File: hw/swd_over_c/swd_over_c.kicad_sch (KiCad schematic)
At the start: 16 parts, among them J1 USB_C_Receptacle_USB2.0, J2 Conn_ARM_JTAG_SWD_10, P1 USB_C_Plug, U1 ATtiny24-20M

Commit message: Somehow got the values for R4 and R5 swapped...
Swapped them in schematic and in code (manually reworked v1.6 boards to swap R4/R5)
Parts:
- R4: value 56k -> 10k; MPN RC0402FR-0756KL -> RC0402FR-0710KL; Vendor Part Number 311-56.0KLRCT-ND -> 311-10.0KLRCT-ND
- R5: value 10k -> 56k; MPN RC0402FR-0710KL -> RC0402FR-0756KL; Vendor Part Number 311-10.0KLRCT-ND -> 311-56.0KLRCT-ND
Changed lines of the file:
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@@
   (title_block
     (title "Debugotron - SWD2USBC")
-    (date "2022-05-15")
-    (rev "1.4")
+    (date "2022-06-07")
+    (rev "1.7")
     (company "Quesadillon LLC")
   )
@@
     (in_bom yes) (on_board yes)
     (property "Reference" "R5" (id 0) (at 180.34 67.31 90))
-    (property "Value" "10k" (id 1) (at 180.34 71.12 90))
+    (property "Value" "56k" (id 1) (at 180.34 71.12 90))
     (property "Footprint" "Resistor_SMD:R_0402_1005Metric" (id 2) (at 180.34 73.66 0)
       (effects (font (size 1.27 1.27)) hide)
@@
       (effects (font (size 1.27 1.27)) hide)
     )
-    (property "Description" "RES 10K OHM 1% 1/16W 0402" (id 4) (at 180.34 73.66 0)
+    (property "Description" "RES 56K OHM 1% 1/16W 0402" (id 4) (at 180.34 73.66 0)
       (effects (font (size 1.27 1.27)) hide)
     )
@@
       (effects (font (size 1.27 1.27)) hide)
     )
-    (property "MPN" "RC0402FR-0710KL" (id 6) (at 180.34 73.66 0)
+    (property "MPN" "RC0402FR-0756KL" (id 6) (at 180.34 73.66 0)
       (effects (font (size 1.27 1.27)) hide)
     )
@@
       (effects (font (size 1.27 1.27)) hide)
     )
-    (property "Vendor Part Number" "311-10.0KLRCT-ND" (id 9) (at 180.34 73.66 0)
+    (property "Vendor Part Number" "311-56.0KLRCT-ND" (id 9) (at 180.34 73.66 0)
       (effects (font (size 1.27 1.27)) hide)
     )
@@
     (in_bom yes) (on_board yes)
     (property "Reference" "R4" (id 0) (at 180.34 66.04 90))
-    (property "Value" "56k" (id 1) (at 180.34 63.5 90))
+    (property "Value" "10k" (id 1) (at 180.34 63.5 90))
     (property "Footprint" "Resistor_SMD:R_0402_1005Metric" (id 2) (at 180.34 60.96 0)
       (effects (font (size 1.27 1.27)) hide)
@@
       (effects (font (size 1.27 1.27)) hide)
     )
-    (property "Description" "RES 56K OHM 1% 1/16W 0402" (id 4) (at 180.34 60.96 0)
+    (property "Description" "RES 10K OHM 1% 1/16W 0402" (id 4) (at 180.34 60.96 0)
       (effects (font (size 1.27 1.27)) hide)
     )
@@
       (effects (font (size 1.27 1.27)) hide)
     )
-    (property "MPN" "RC0402FR-0756KL" (id 6) (at 180.34 60.96 0)
+    (property "MPN" "RC0402FR-0710KL" (id 6) (at 180.34 60.96 0)
       (effects (font (size 1.27 1.27)) hide)
     )
@@
       (effects (font (size 1.27 1.27)) hide)
     )
-    (property "Vendor Part Number" "311-56.0KLRCT-ND" (id 9) (at 180.34 60.96 0)
+    (property "Vendor Part Number" "311-10.0KLRCT-ND" (id 9) (at 180.34 60.96 0)
       (effects (font (size 1.27 1.27)) hide)
     )
@@
     )
     (path "/58dcbd1f-c6fe-4c32-b2f3-448aeeb2a148"
-      (reference "R4") (unit 1) (value "56k") (footprint "Resistor_SMD:R_0402_1005Metric")
+      (reference "R4") (unit 1) (value "10k") (footprint "Resistor_SMD:R_0402_1005Metric")
     )
     (path "/4270b08b-df31-4c02-8549-8caf041f455d"
-      (reference "R5") (unit 1) (value "10k") (footprint "Resistor_SMD:R_0402_1005Metric")
+      (reference "R5") (unit 1) (value "56k") (footprint "Resistor_SMD:R_0402_1005Metric")
     )
     (path "/28b61970-be32-4027-a006-7ee2adc035c1"

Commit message: v2.0 SWD Over C
Going to a different MCU since it's available at JLC and both USB-C connectors instead of plugs.
_maybe_ this will work with a short USBC cable with all the conductors and make things much easier
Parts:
- removed J1: USB_C_Receptacle_USB2.0, alvarop:USB4500-03, symbol Connector:USB_C_Receptacle_USB2.0
- removed P1: USB_C_Plug, alvarop:‎USB4155-03-C‎, symbol Connector:USB_C_Plug
- added J1, J3: USB_C_Receptacle, alvarop:MOLEX-1054500101, symbol Connector:USB_C_Receptacle
- U1: footprint ultralibrarian:ATTINY24A-MMH_MOD -> ultralibrarian:ATTINY24A-MU; MPN ATTINY24A-MMH -> ATTINY24A-MU; Vendor Part Number ATTINY24A-MMH-ND -> ATTINY24A-MU-ND
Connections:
- net CC1: now also J3.A5 (CC1)
- net CC1_IN_MOSI: now also J1.A5 (CC1)
- net CC1_R1: now also U1.5 (AREF/PA0); no longer U1.11 (XTAL1/PB0)
- net CC1_R2: now also U1.4 (PA1); no longer U1.12 (XTAL2/PB1)
- net CC2: now also J3.B5 (CC2)
- net CC2_IN_MISO: now also J1.B5 (CC2)
- net CC2_R1: now also U1.12 (XTAL2/PB1); no longer U1.4 (PA1)
- net CC2_R2: now also U1.11 (XTAL1/PB0); no longer U1.5 (AREF/PA0)
- net D+: now also J1.A6 (D+), J1.B6 (D+), J3.A6 (D+), J3.B6 (D+)
- net D-: now also J1.A7 (D-), J1.B7 (D-), J3.A7 (D-), J3.B7 (D-)
- net GND: now also J1.A1 (GND), J1.A12 (GND), J1.B1 (GND), J1.B12 (GND), J3.A1 (GND), J3.A12 (GND), J3.B1 (GND), J3.B12 (GND)
- net MCURST: now also J1.B8 (SBU2)
- net NRST: now also J3.A11 (RX2+)
- net SBU1: now also J3.A8 (SBU1)
- net SBU2: now also J3.B8 (SBU2)
- net SCK: now also J1.A8 (SBU1)
- net SHIELD: now also J1.S1 (SHIELD), J3.S1 (SHIELD)
- net SWDCLK: now also J3.B10 (RX1-)
- net SWDIO: now also J3.B11 (RX1+)
- net SWO: now also J3.A10 (RX2-)
- net VBUS: now also J1.A4 (VBUS), J1.A9 (VBUS), J1.B4 (VBUS), J1.B9 (VBUS), J3.A4 (VBUS), J3.A9 (VBUS), J3.B4 (VBUS), J3.B9 (VBUS)

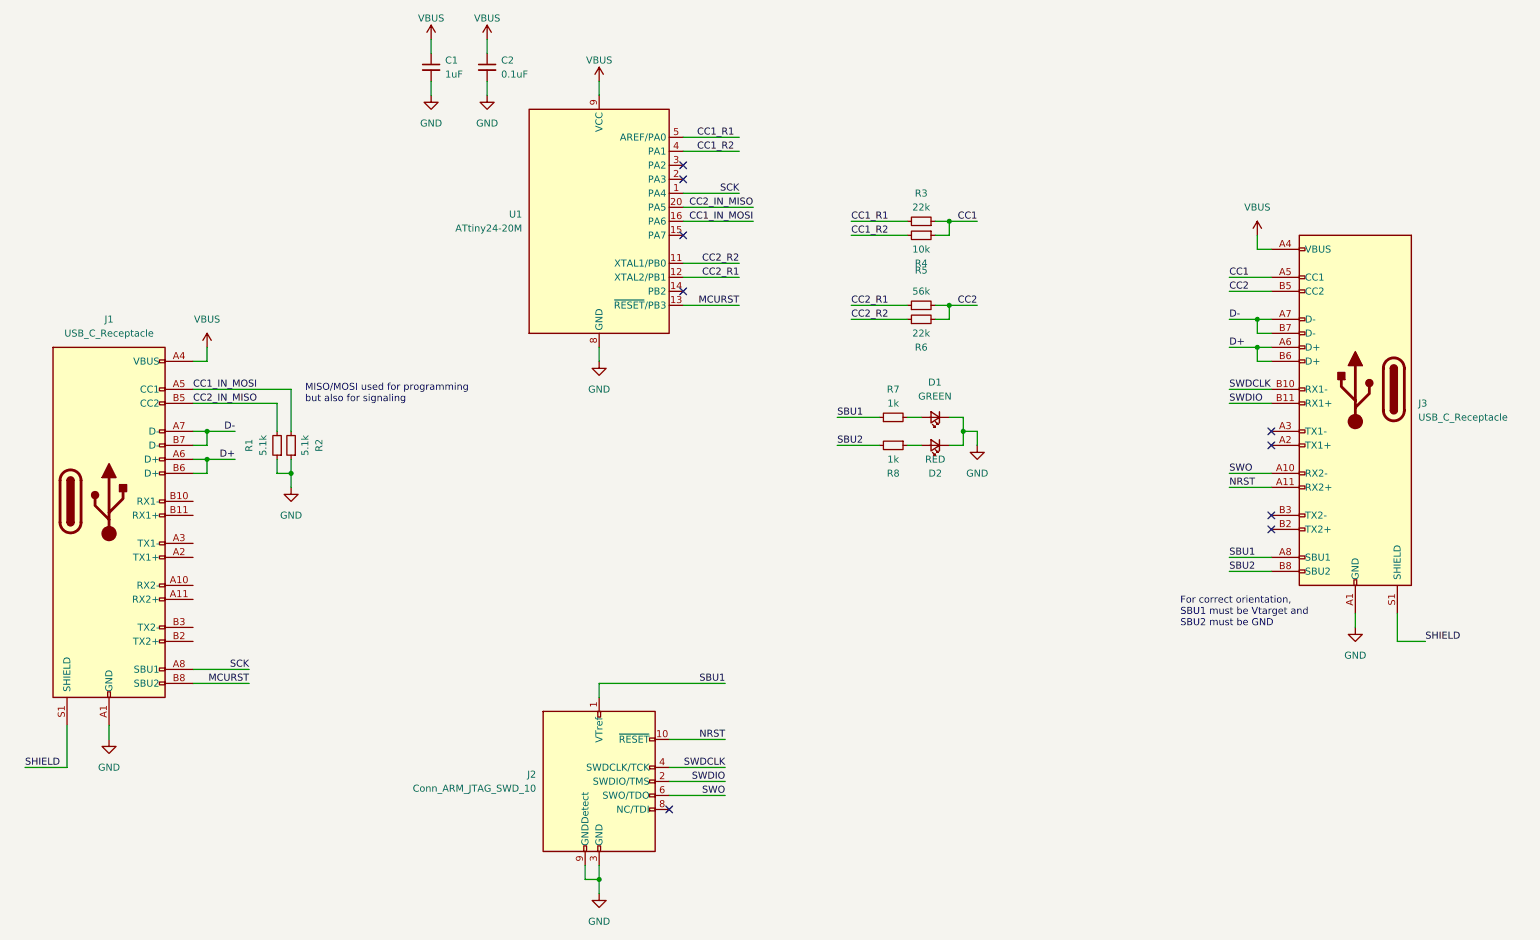
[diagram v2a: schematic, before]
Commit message: v3.0 SWD2USBC
Had the tx/rx pairs flipped since I switched from USB-C Plug to Connector...
Removed MCU since cables don't connect both CC1/CC2 so can't actually do a proper debug accessory mode.
Should still work though?
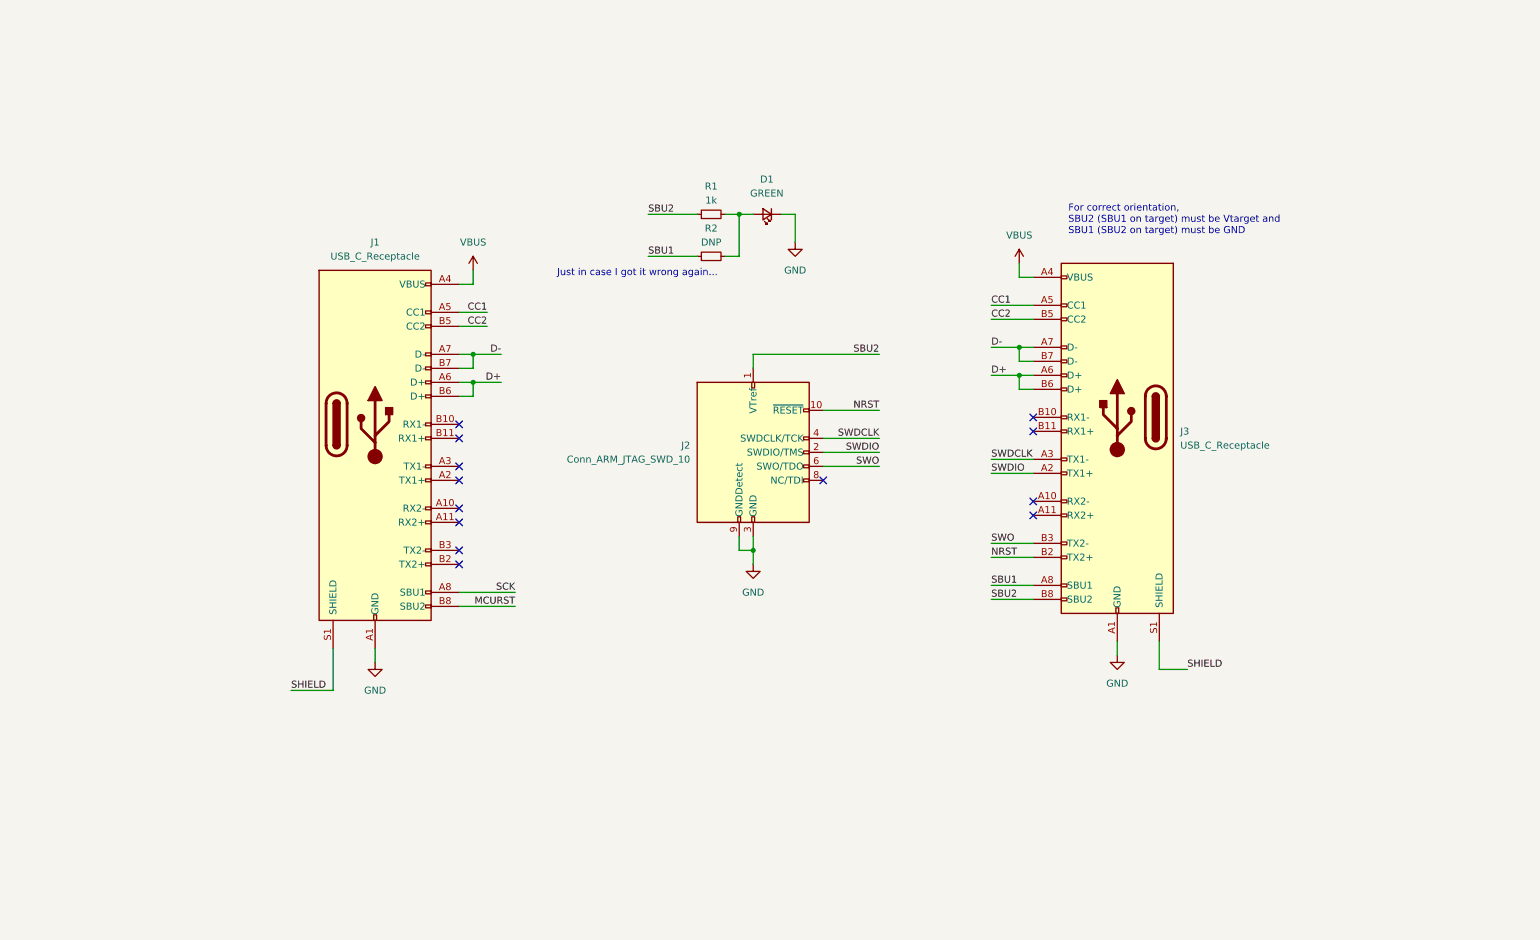
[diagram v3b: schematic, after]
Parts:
- removed C1: 1uF, Capacitor_SMD:C_0402_1005Metric, symbol Device:C_Small
- removed C2: 0.1uF, Capacitor_SMD:C_0402_1005Metric, symbol Device:C_Small
- removed D2: RED, LED_SMD:LED_0603_1608Metric, symbol Device:LED_Small
- removed R1: 5.1k, Resistor_SMD:R_0402_1005Metric, symbol Device:R_Small
- removed R3, R6: 22k, Resistor_SMD:R_0402_1005Metric, symbol Device:R_Small
- removed R4: 10k, Resistor_SMD:R_0402_1005Metric, symbol Device:R_Small
- removed R5: 56k, Resistor_SMD:R_0402_1005Metric, symbol Device:R_Small
- removed R8: 1k, Resistor_SMD:R_0402_1005Metric, symbol Device:R_Small
- removed U1: ATtiny24-20M, ultralibrarian:ATTINY24A-MU, symbol MCU_Microchip_ATtiny:ATtiny24-20M
- R2: value 5.1k -> DNP; MPN RC0402FR-075K1L -> RC0402FR-071KL; Vendor Part Number 311-5.1KJRCT-ND -> 311-1.00KLRCT-ND
- renumbered R7 to R1
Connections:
- net CC2_IN_MISO is gone; now on net CC2: J1.B5 (CC2)
- net CC1: now also J1.A5 (CC1)
- net GND: no longer R2.1
- net NRST: now also J3.B2 (TX2+); no longer J3.A11 (RX2+)
- net SBU1: now also R2.1; no longer J2.1 (VTref), R1.1
- net SBU2: now also J2.1 (VTref), R1.1
- net SWDCLK: now also J3.A3 (TX1-); no longer J3.B10 (RX1-)
- net SWDIO: now also J3.A2 (TX1+); no longer J3.B11 (RX1+)
- net SWO: now also J3.B3 (TX2-); no longer J3.A10 (RX2-)
- net at D1.2 (A), R1.2: now also R2.2
- removed net CC1_IN_MOSI: J1.A5 (CC1), R2.2
- no-connect marks 9 -> 13
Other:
- note added: "For correct orientation, SBU2 (SBU1 on target) must be Vtarget and SBU1 (SBU2 on target) must be GND"
- note added: "Just in case I got it wrong again..."
- note removed: "For correct orientation, SBU1 must be Vtarget and SBU2 must be GND"
- note removed: "MISO/MOSI used for programming but also for signaling"
- moved on the sheet: D1, J1, J2, J3, R1

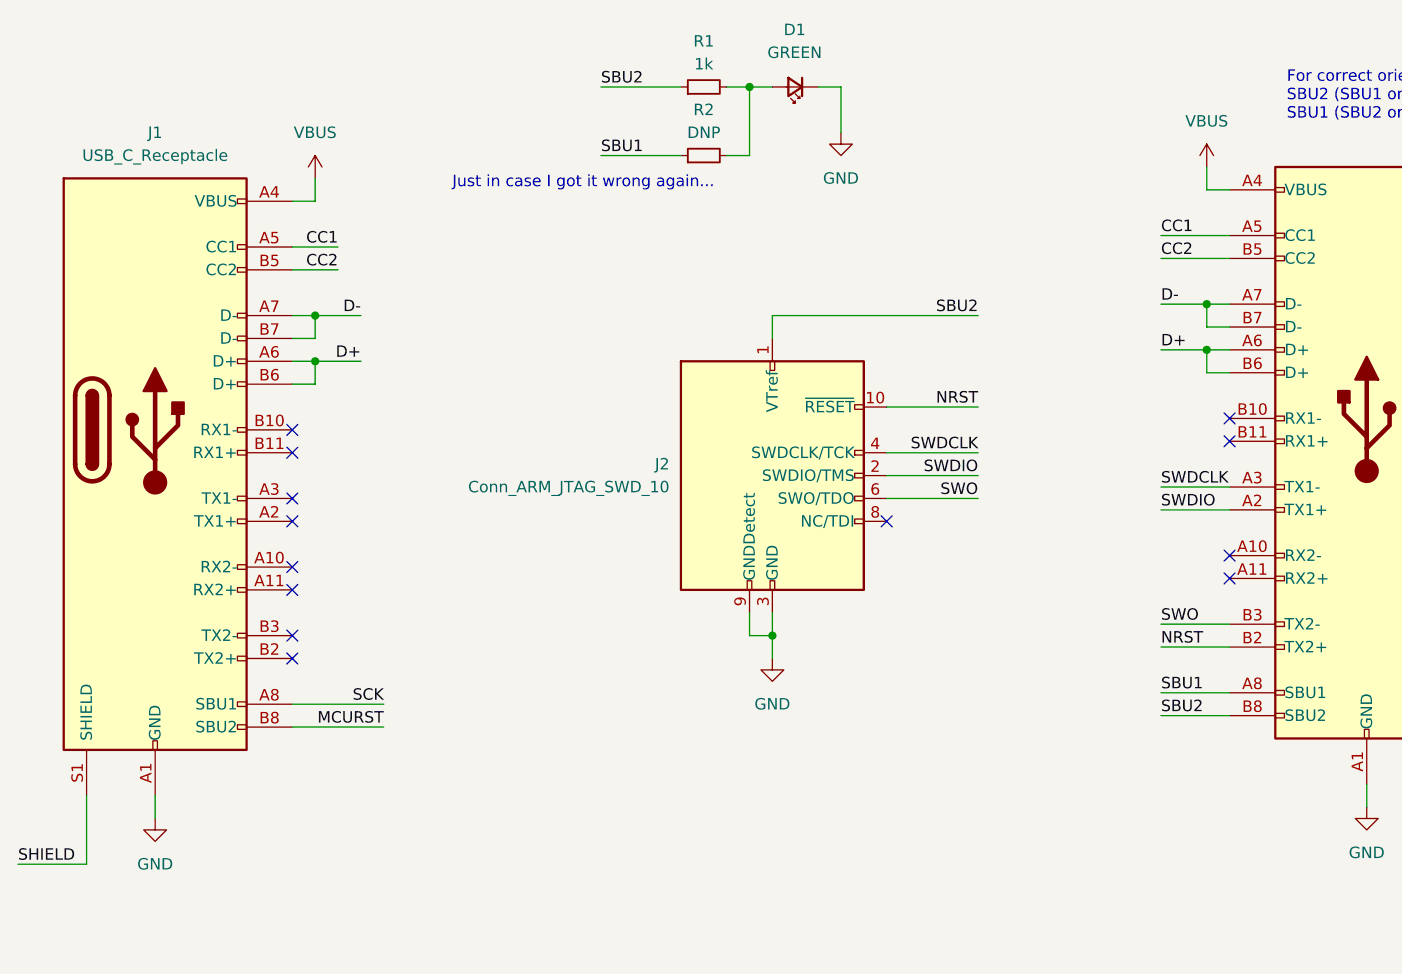
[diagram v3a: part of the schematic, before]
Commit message: Release SWD over C v4.0
Swapped Tx/Rx lines since USB C cables cross them over...
Thanks to Matthias for reporting the bug!
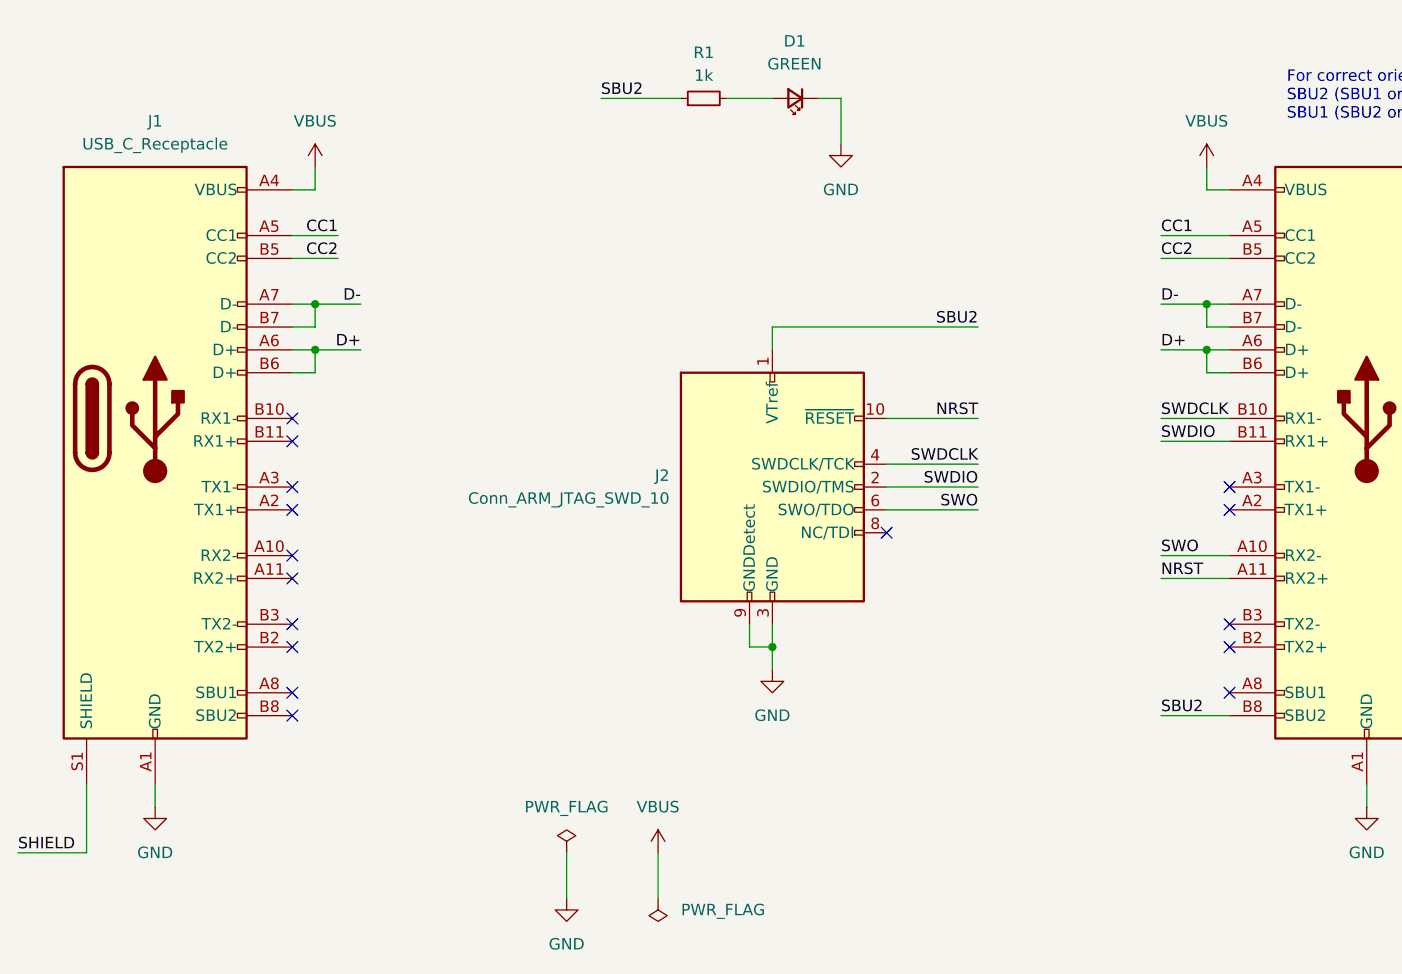
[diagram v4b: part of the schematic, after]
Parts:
- removed R2: DNP, Resistor_SMD:R_0402_1005Metric, symbol Device:R_Small
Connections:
- net NRST: now also J3.A11 (RX2+); no longer J3.B2 (TX2+)
- net SWDCLK: now also J3.B10 (RX1-); no longer J3.A3 (TX1-)
- net SWDIO: now also J3.B11 (RX1+); no longer J3.A2 (TX1+)
- net SWO: now also J3.A10 (RX2-); no longer J3.B3 (TX2-)
- net MCURST: no longer names the net of J1.B8 (SBU2)
- net SBU1: no longer names the net of J3.A8 (SBU1)
- net SCK: no longer names the net of J1.A8 (SBU1)
- no-connect marks 13 -> 16
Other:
- note removed: "Just in case I got it wrong again..."
- moved on the sheet: D1, J1, J2, R1
